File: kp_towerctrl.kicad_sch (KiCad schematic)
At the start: 15 parts, among them J1 ext_5v, J2 Conn_02x05_Counter_Clockwise, J3 Conn_02x05_Counter_Clockwise, J4 Conn_02x05_Counter_Clockwise, J5 Conn_02x05_Counter_Clockwise, J6 Conn_02x05_Counter_Clockwise, U1 Teensy4.0, U2 MCP23S17_SP, U3 MCP23S17_SP, U4 MCP3008

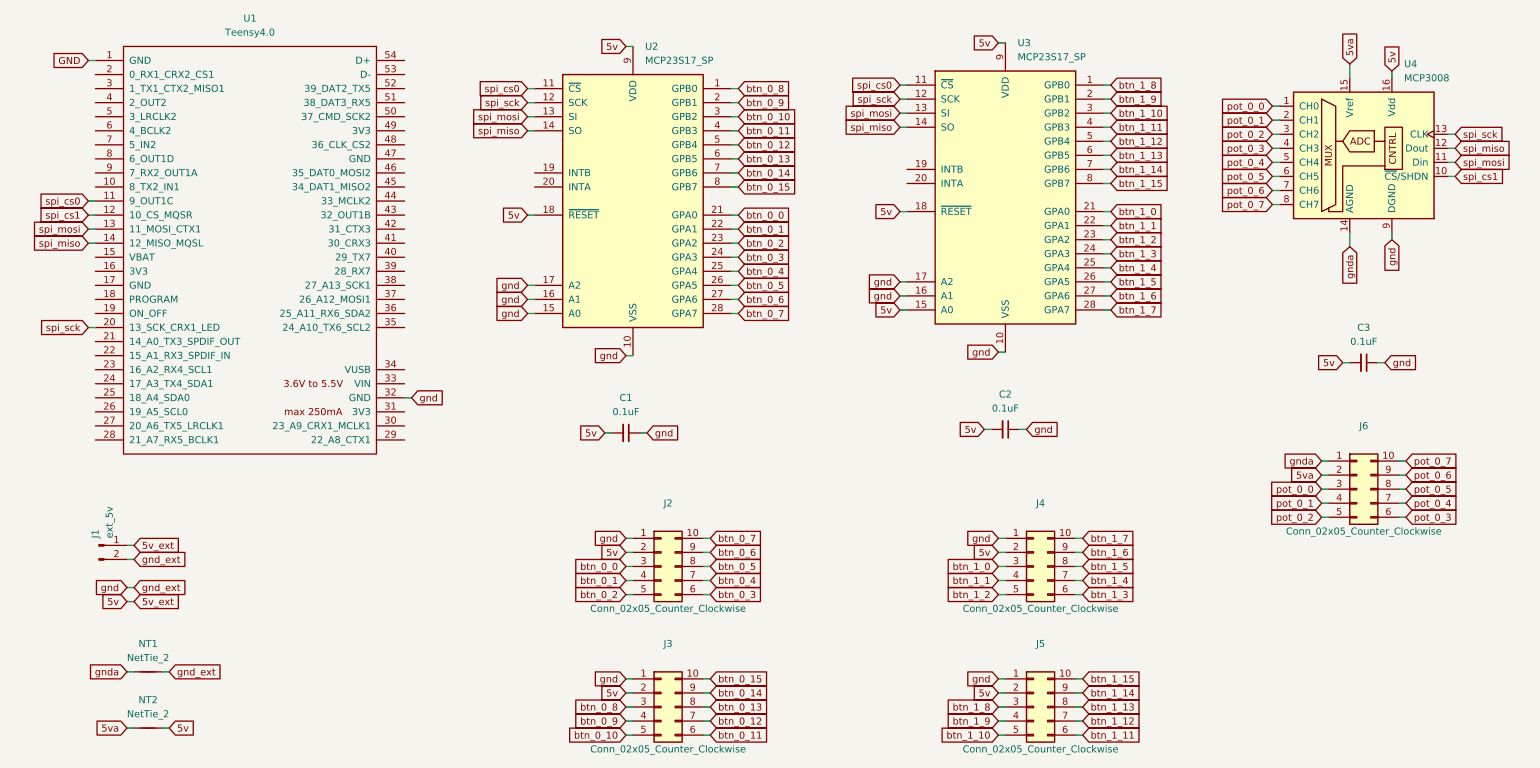
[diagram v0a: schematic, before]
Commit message: connect 3.3v
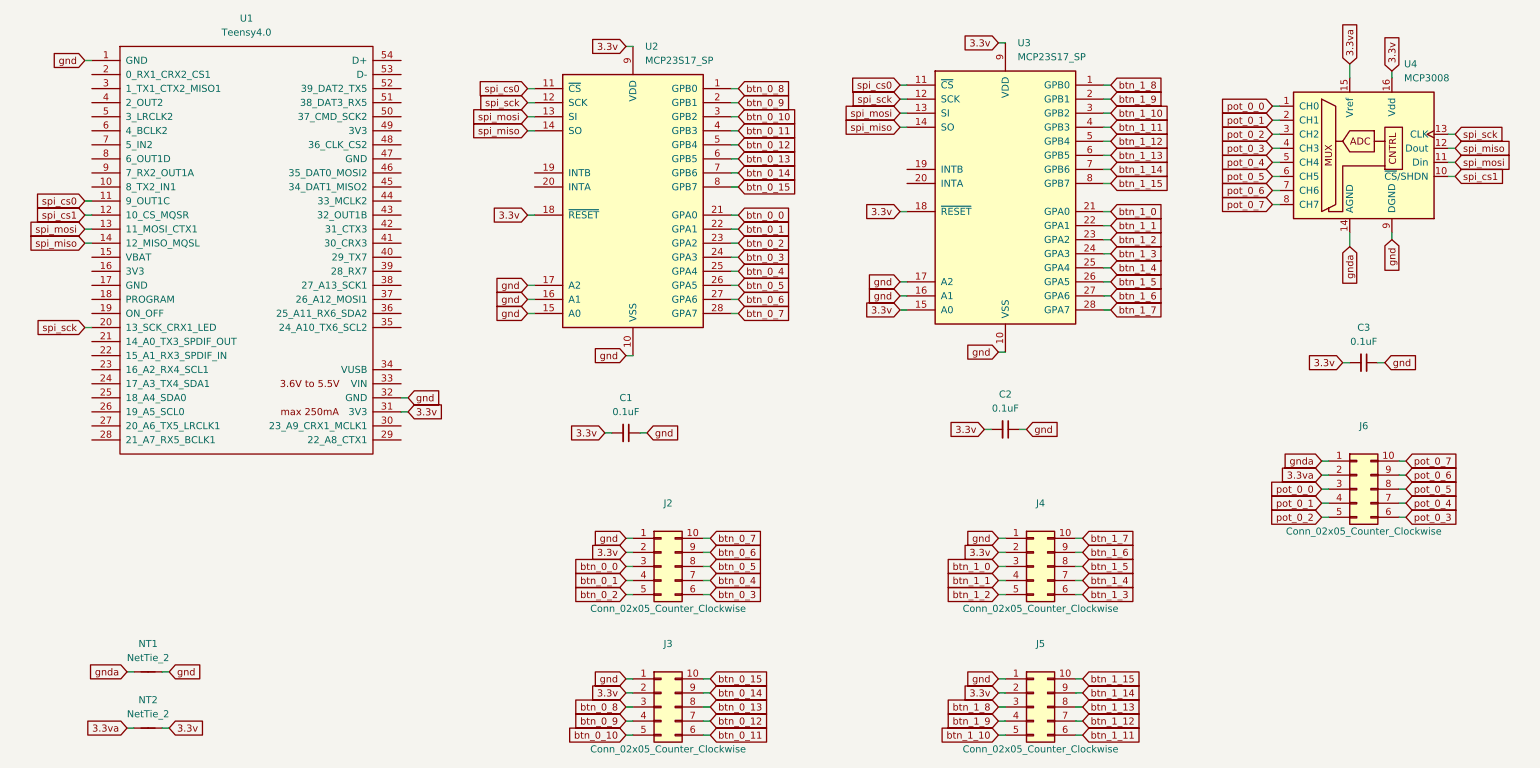
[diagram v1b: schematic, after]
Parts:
- removed J1: ext_5v, Connector_PinHeader_2.54mm:PinHeader_1x02_P2.54mm_Vertical, symbol Connector:Conn_01x02_Pin
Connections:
- net 5v is gone; now on net 3.3v: C1.2, C2.2, C3.2, J2.2 (Pin_2), J3.2 (Pin_2), J4.2 (Pin_2), J5.2 (Pin_2), NT2.2, U2.18 (~{RESET}), U2.9 (VDD), U3.15 (A0), U3.18 (~{RESET}), U3.9 (VDD), U4.16 (Vdd)
- net GND is gone; now on net gnd: U1.1 (GND)
- net 3.3v: now reaches U1.31 (3V3)
- net 5va renamed 3.3va
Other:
- moved on the sheet: U1
